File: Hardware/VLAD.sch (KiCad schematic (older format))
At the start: 30 parts, among them J1 BMP388, J2 BNO055, J5 Conn_01x03_Male, Q1 MMDT2222A, Q2 MMDT2222A, U1 ESP32-WROOM-32

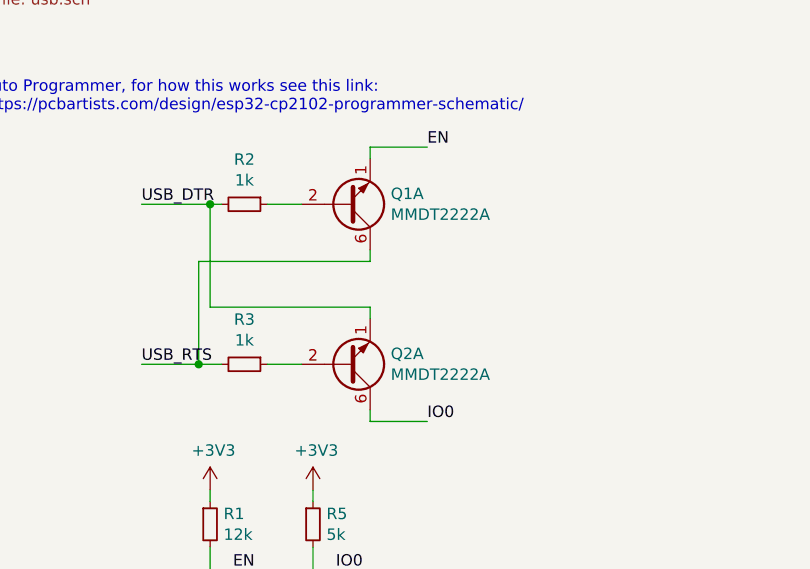
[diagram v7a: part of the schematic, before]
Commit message: Traccs done, meme time
Need to fix the silkscreen stuff for the components and also the back silkscreen memes etc.
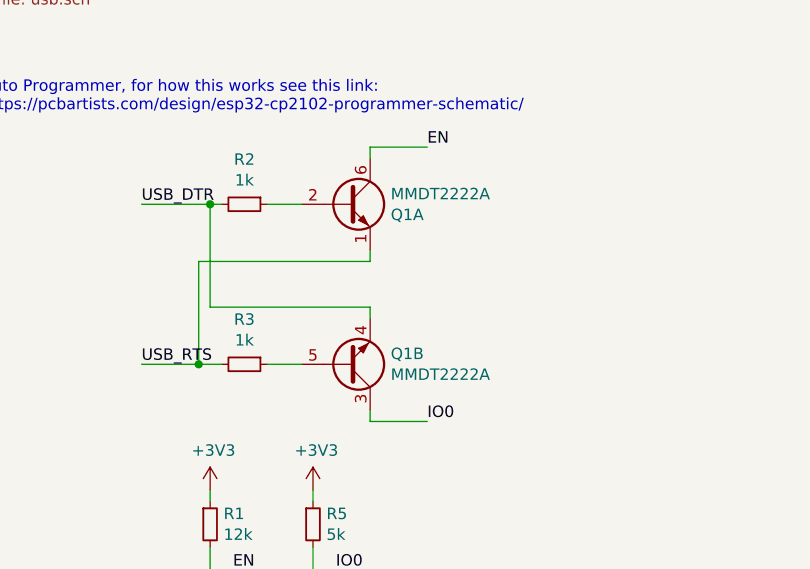
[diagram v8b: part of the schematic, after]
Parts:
- removed Q2: MMDT2222A, Package_TO_SOT_SMD:SOT-363_SC-70-6, symbol Transistor_BJT:MMDT2222A
- added unit 2 of Q1
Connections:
- net EN: now also Q1.6 (C1); no longer Q1.1 (E1)
- net IO0: now also Q1.3 (C2)
- net USB_DTR: now also Q1.4 (E2)
- net USB_RTS: now also Q1.1 (E1); no longer Q1.6 (C1)
- net at R3.1: now also Q1.5 (B2)
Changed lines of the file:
@@
-$EndComp
-$Comp
-L Transistor_BJT:MMDT2222A Q2
-U 1 1 60B6FFE0
-P 2350 4800
-F 0 "Q2" H 2540 4754 50  0000 L CNN
-F 1 "MMDT2222A" H 2540 4845 50  0000 L CNN
-F 2 "Package_TO_SOT_SMD:SOT-363_SC-70-6" H 2550 4900 50  0001 C CNN
-F 3 "http://www.diodes.com/_files/datasheets/ds30125.pdf" H 2350 4800 50  0001 C CNN
-	1    2350 4800
-	1    0    0    1
 $EndComp
 $Comp
@@
 F 3 "http://www.diodes.com/_files/datasheets/ds30125.pdf" H 2350 4100 50  0001 C CNN
 	1    2350 4100
+	1    0    0    -1
+$EndComp
+$Comp
+L Transistor_BJT:MMDT2222A Q1
+U 2 1 60BEDD25
+P 2350 4800
+F 0 "Q1" H 2540 4754 50  0000 L CNN
+F 1 "MMDT2222A" H 2540 4845 50  0000 L CNN
+F 2 "Package_TO_SOT_SMD:SOT-363_SC-70-6" H 2550 4900 50  0001 C CNN
+F 3 "http://www.diodes.com/_files/datasheets/ds30125.pdf" H 2350 4800 50  0001 C CNN
+	2    2350 4800
 	1    0    0    1
 $EndComp
